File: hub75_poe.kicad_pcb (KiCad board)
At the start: 4 copper layers, 70.5 x 48.3 mm, 104 parts, among them J1 0826-1X1T-JK-F, J2 Conn_02x08_Odd_Even, J3 7466003R, J4 502382-0970, J5 7466003R, Q1 FDS2582, SW1 434133025816, T1 PA2369NL, U1 KSZ8081MLX, U10 SN74LVC8T245, U11 SN74LVC8T245, U12 ASEMB-100.000MHZ-LY-T, U13 VO615A, U14 TL431PK, U2 ICE40HX8K-BG121, U3 NCP1081, U4 TPS74633, U5 TPS74612, U6 W25Q32JVSS, U7 S27KL0641, U8 ASEMB-25.000MHZ-LC-T, U9 TPS74618

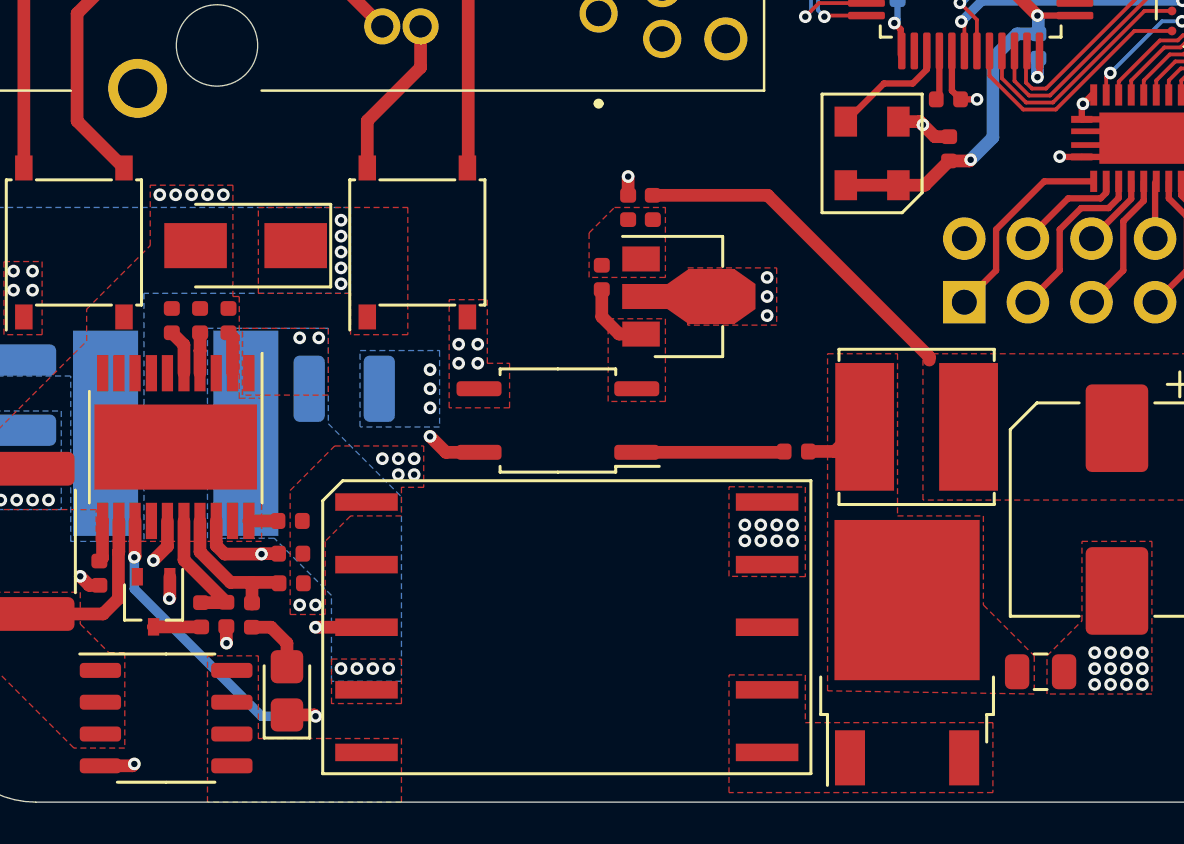
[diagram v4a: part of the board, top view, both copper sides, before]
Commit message: Add missing detection resistor
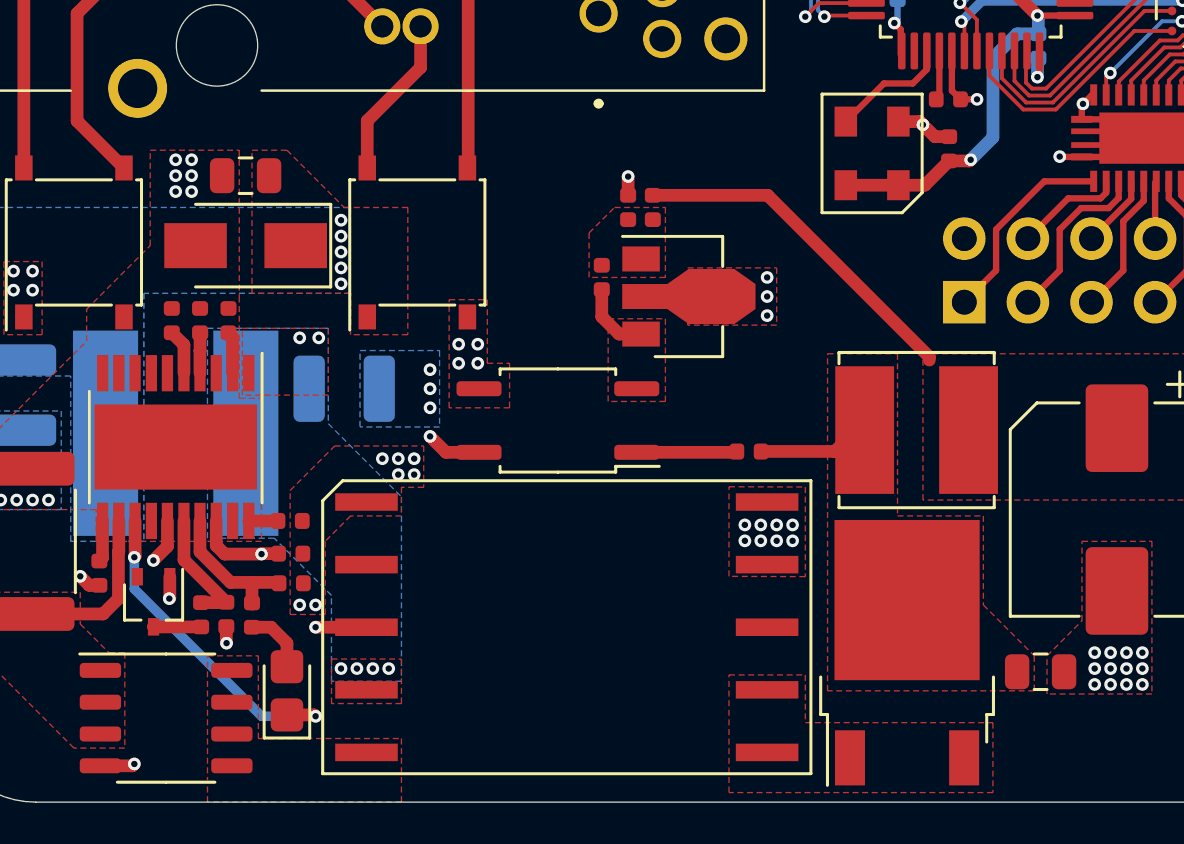
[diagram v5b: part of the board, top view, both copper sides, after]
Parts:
- added R12: 25.5k, Resistor_SMD:R_0805_2012Metric, F.Cu at (126.5, 75.3)
- C10, C11, C41: value C -> 2.2uf
- C6: value C -> 470nf
- C7: value C -> 2.2uF
- C8: value C -> 4.7uf
- C9: value C -> 4.7nf
- L2: value L -> 6.8uH
- R10, R11: value R -> 1k
- R2: value R -> 30.9
- R3: value R -> 100k
- R4: value R -> 56k
- R5, R9: value R -> 330
- R6: value R -> 200k
- R7: value R -> 50
- R8: value R -> 33m
- moved R9 1.89 mm to (146.6, 86.3)
- moved L1 0.13 mm to (153.3, 85.5)
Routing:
- net Net-(C12-Pad1): track 2.34 -> 4.23 mm
- net Net-(R9-Pad2): track 5.90 -> 4.01 mm
- net GNDPWR: vias 25 -> 26
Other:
- board text added: "NO LICK SCIENCE (approx. 60 VDC)"
- board text removed: "DO NOT LICK THIS SCIENCE (60V DC)"

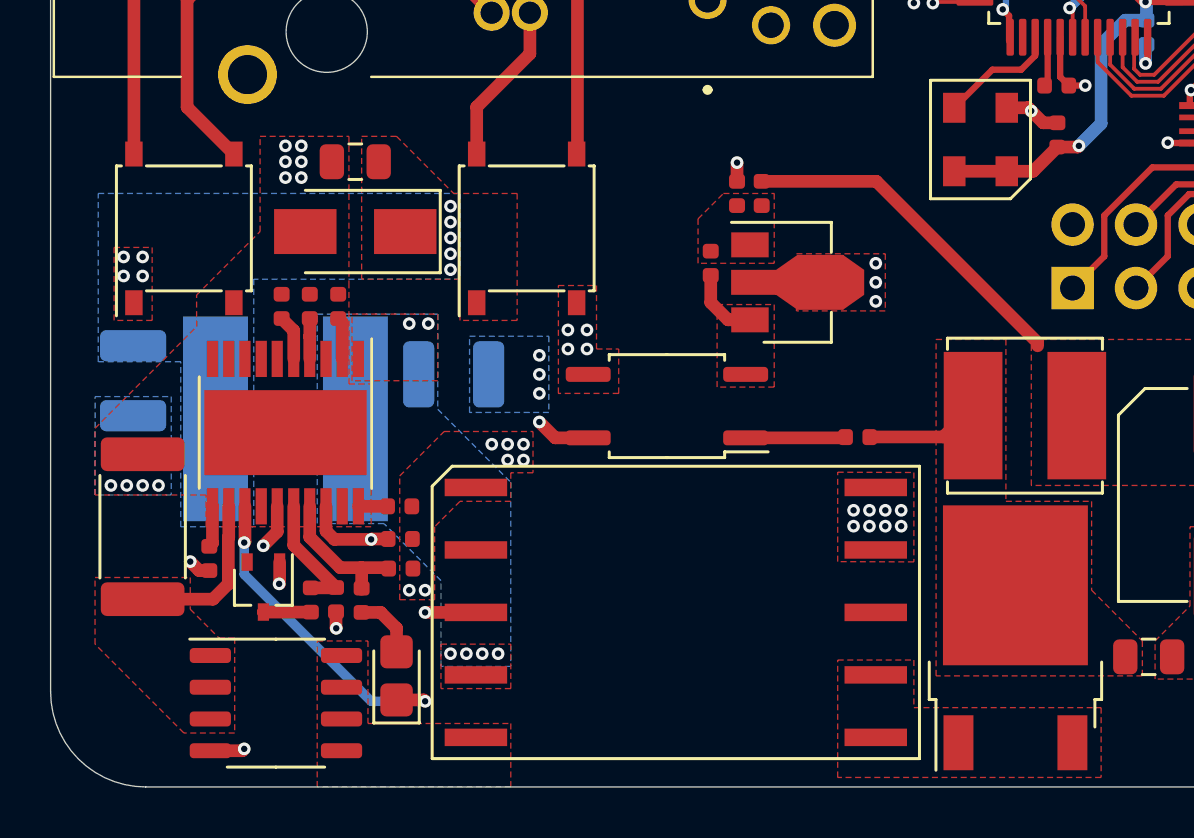
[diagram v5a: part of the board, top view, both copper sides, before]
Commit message: More routing cleanup
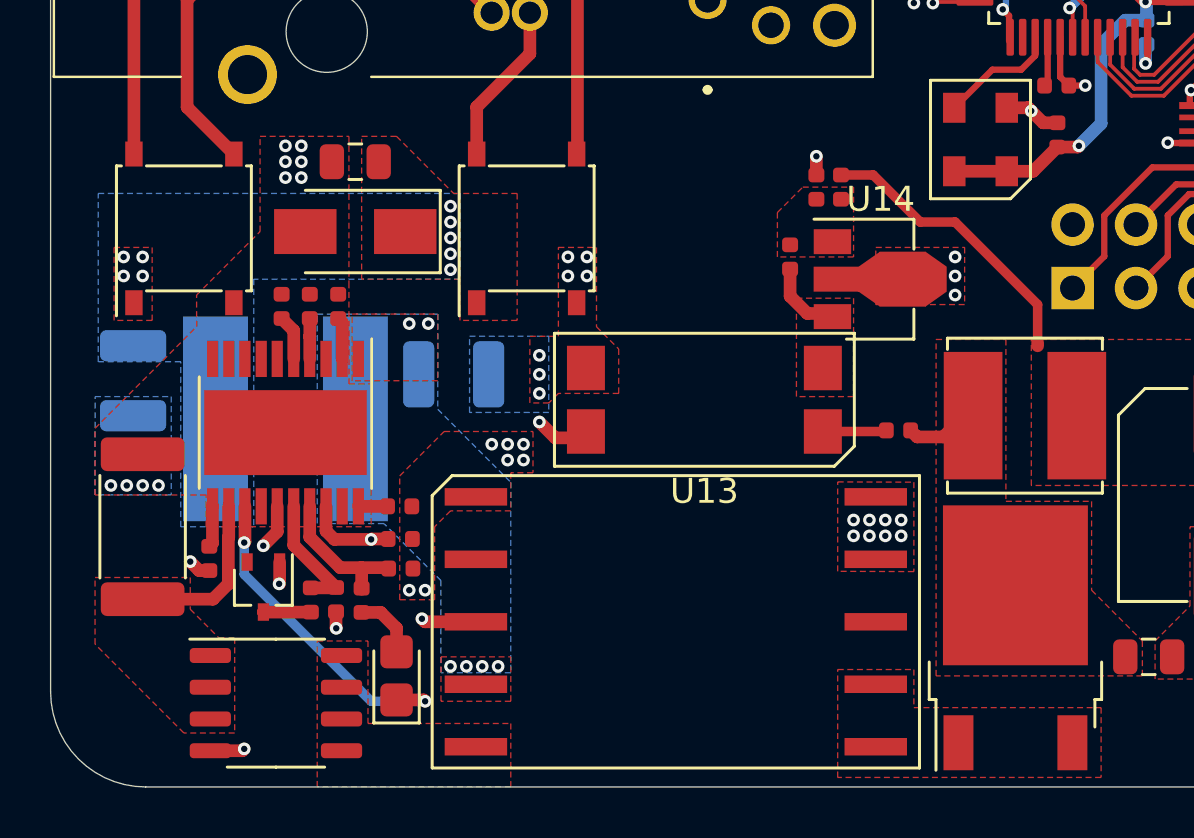
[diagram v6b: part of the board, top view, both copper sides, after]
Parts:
- U13: footprint Package_SO:SO-4_4.4x3.9mm_P2.54mm -> hub75_poe:VO615A-9X017T
- moved U14 3.30 mm to (147.1, 80.0)
- moved R10 3.19 mm to (145.9, 76.3)
- moved R11 3.19 mm to (144.9, 76.3)
- moved C41 3.19 mm to (143.9, 79.1)
- moved R9 1.65 mm to (148.2, 86.1)
- moved U13 1.52 mm to (140.5, 84.8), turned to 90 degrees
- moved T1 0.38 mm to (139.3, 93.7)
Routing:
- net VBUS: track 18.7 -> 16.5 mm
- net Net-(C12-Pad1): track 4.23 -> 2.70 mm
- net Net-(R9-Pad2): track 4.01 -> 2.56 mm
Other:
- rule pad_to_mask_clearance: 0.05 -> 0
- board text added: "PROJECT LIGHTNING PACKET ${GIT_REV} UNTESTED"
- board text removed: "PROJECT LIGHTNING PACKET R0.75 UNTESTED"

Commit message: Fix SOT-89-3 footprint
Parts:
- U14: footprint Package_TO_SOT_SMD:SOT-89-3 -> hub75_poe:SOT-89-3
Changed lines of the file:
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@@
-(kicad_pcb (version 20200614) (host pcbnew "5.99.0-unknown-b48a627~101~ubuntu20.04.1")
+(kicad_pcb (version 20200614) (host pcbnew "5.99.0-unknown-19b7755~101~ubuntu20.04.1")
   (general
     (thickness 1.6)
@@
     (add_net "/SPARE_B")
   )
-  (module "Package_TO_SOT_SMD:SOT-89-3" (layer "F.Cu")
+  (module "hub75_poe:SOT-89-3" (layer "F.Cu")
     (at 147.066 80.01)
     (descr "SOT-89-3")
@@
       (effects (font (size 0.6 0.6) (thickness 0.09)))
     )
-    (pad "2" smd trapezoid (at -0.0762 0 90) (size 1.5 1) (rect_delta 0 0.7 ) (layers "F.Cu" "F.Paste" "F.Mask")
+    (pad "2" smd trapezoid (at -0.0762 0 270) (size 1.5 1) (rect_delta 0 0.7 ) (layers "F.Cu" "F.Paste" "F.Mask")
       (net 14 "GND") (pinfunction "A"))
     (pad "2" smd rect (at 1.3335 0 270) (size 2.2 1.84) (layers "F.Cu" "F.Paste" "F.Mask")
@@
     (pad "1" smd rect (at -1.48 -1.5 270) (size 1 1.5) (layers "F.Cu" "F.Paste" "F.Mask")
       (net 205 "Net-(C41-Pad2)") (pinfunction "REF"))
-    (pad "2" smd trapezoid (at 2.667 0 270) (size 1.6 0.85) (rect_delta 0 0.6 ) (layers "F.Cu" "F.Paste" "F.Mask")
+    (pad "2" smd trapezoid (at 2.667 0 90) (size 1.6 0.85) (rect_delta 0 0.6 ) (layers "F.Cu" "F.Paste" "F.Mask")
       (net 14 "GND") (pinfunction "A"))
     (model "${KISYS3DMOD}/Package_TO_SOT_SMD.3dshapes/SOT-89-3.wrl"

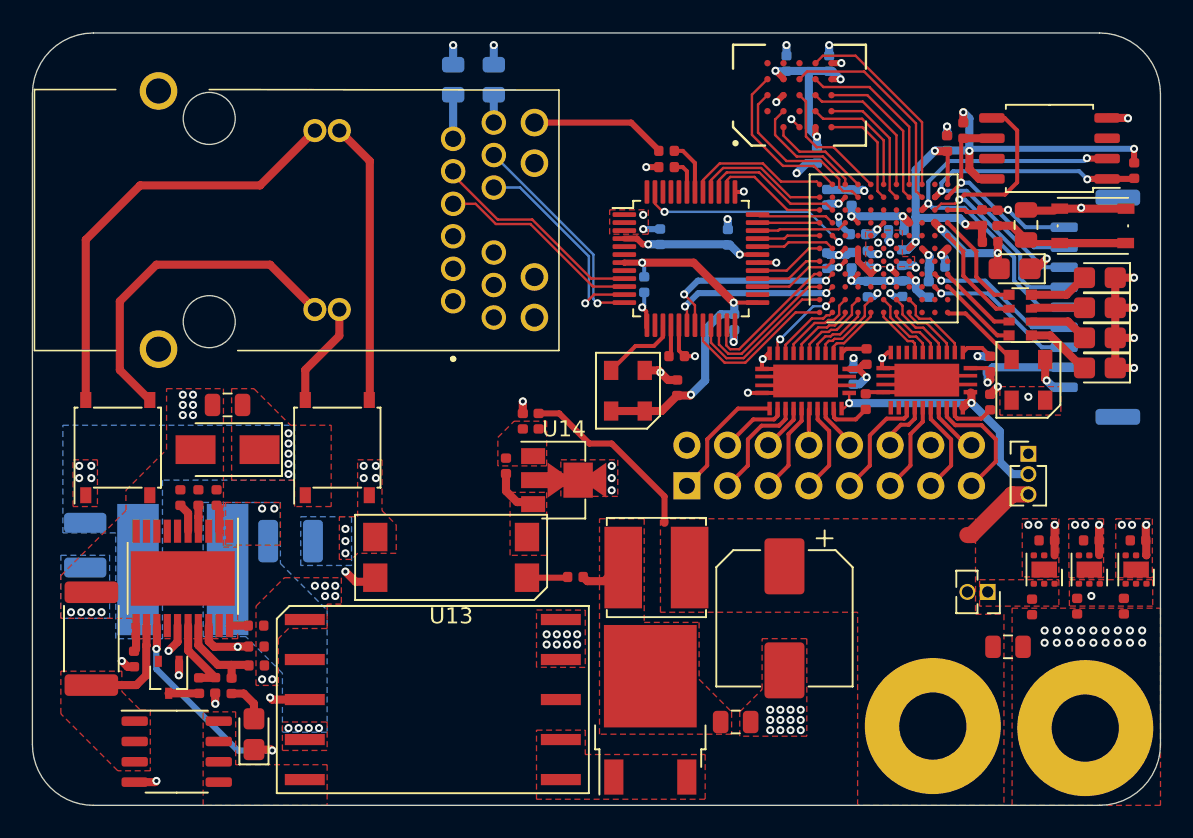
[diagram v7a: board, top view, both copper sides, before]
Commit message: Swap low voltage caps, remove hv side LC filter
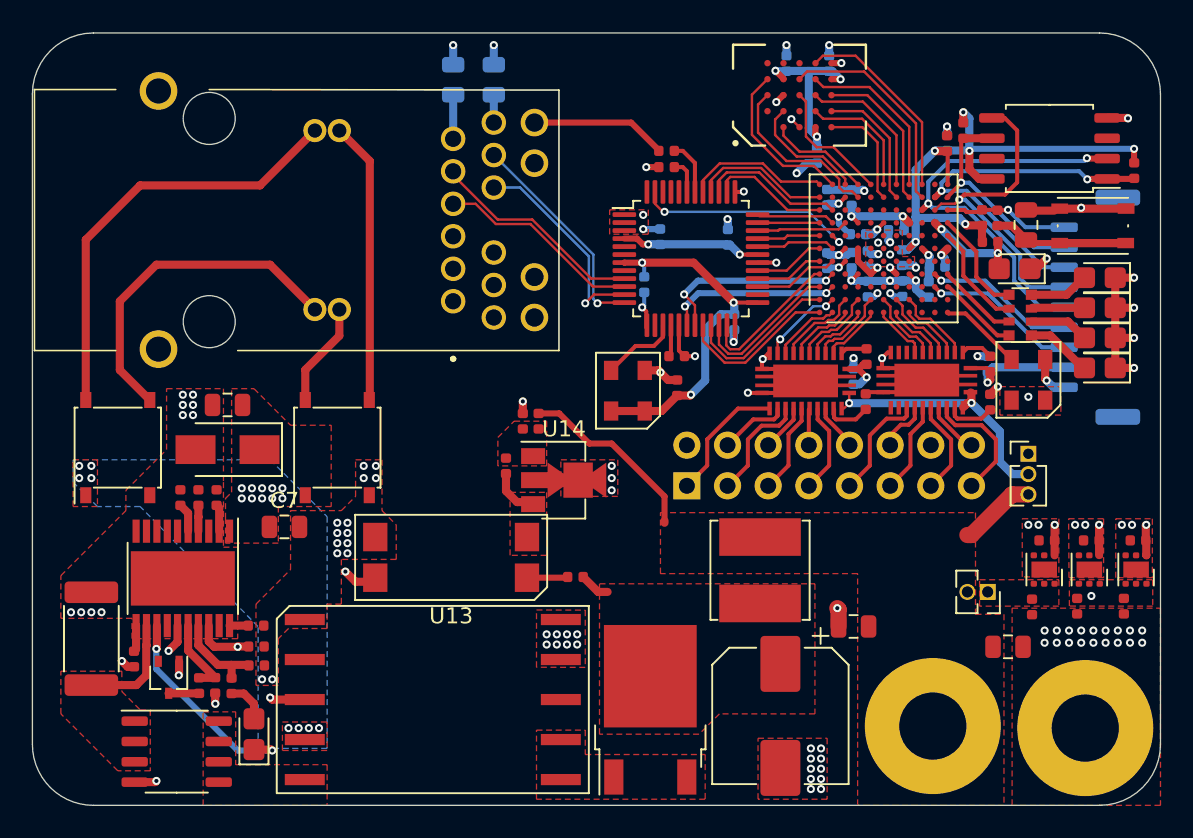
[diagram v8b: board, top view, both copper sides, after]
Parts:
- removed C8: 4.7uf, Capacitor_SMD:C_1210_3225Metric
- removed L2: 6.8uH, Inductor_SMD:L_Bourns-SRN8040_8x8.15mm
- C7: value 2.2uF -> 100nf; footprint Capacitor_SMD:C_1210_3225Metric -> Capacitor_SMD:C_0805_2012Metric; moved to F.Cu
- moved C7 12.5 mm to (130.0, 82.9), turned to 0 degrees
- moved C12 9.48 mm to (165.6, 89.2), turned to 180 degrees
- moved L1 6.48 mm to (159.8, 85.6), turned to 90 degrees
- moved C13 6.10 mm to (161.0, 94.7)
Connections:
- C12 pad 1: Net-(C12-Pad1) -> VBUS
- C13 pad 1: VBUS -> Net-(C13-Pad1)
- D11 pad 2: Net-(C12-Pad1) -> Net-(C13-Pad1)
- L1 pad 1: Net-(C12-Pad1) -> Net-(C13-Pad1)
- R9 pad 1: Net-(C12-Pad1) -> Net-(C13-Pad1)
- T1 pad 2: Net-(C8-Pad1) -> /POE/POE_P
- U3 pad 1: Net-(C8-Pad1) -> /POE/POE_P
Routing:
- net Net-(C12-Pad1): track 2.70 -> 0.00 mm
- net Net-(C13-Pad1): track 0.00 -> 1.91 mm
- net GND: track 66.5 -> 67.6 mm, vias 89 -> 88
- net Net-(C8-Pad1): vias 6 -> 0
- net /POE/POE_P: vias 9 -> 18
- added copper zone on F.Cu, net Net-(C13-Pad1)
- removed copper zone on B.Cu, net GNDPWR
- removed copper zone on F.Cu, net Net-(C12-Pad1)
- removed copper zone on B.Cu, net Net-(C8-Pad1)
- removed copper zone on F.Cu, net Net-(C8-Pad1)
